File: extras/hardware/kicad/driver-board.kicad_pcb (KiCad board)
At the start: 4 copper layers, 42.8 x 36.8 mm, 49 parts, among them J1 Conn_01x13_Male, U1 TXS0108E, U2 ME6210A30M3G, U3 ME6210A33M3G, U4 TLV61046ADB, U5 NC7SZ125, U6 FT813, U7 ER-TFT040-2, X1 YSX321SL

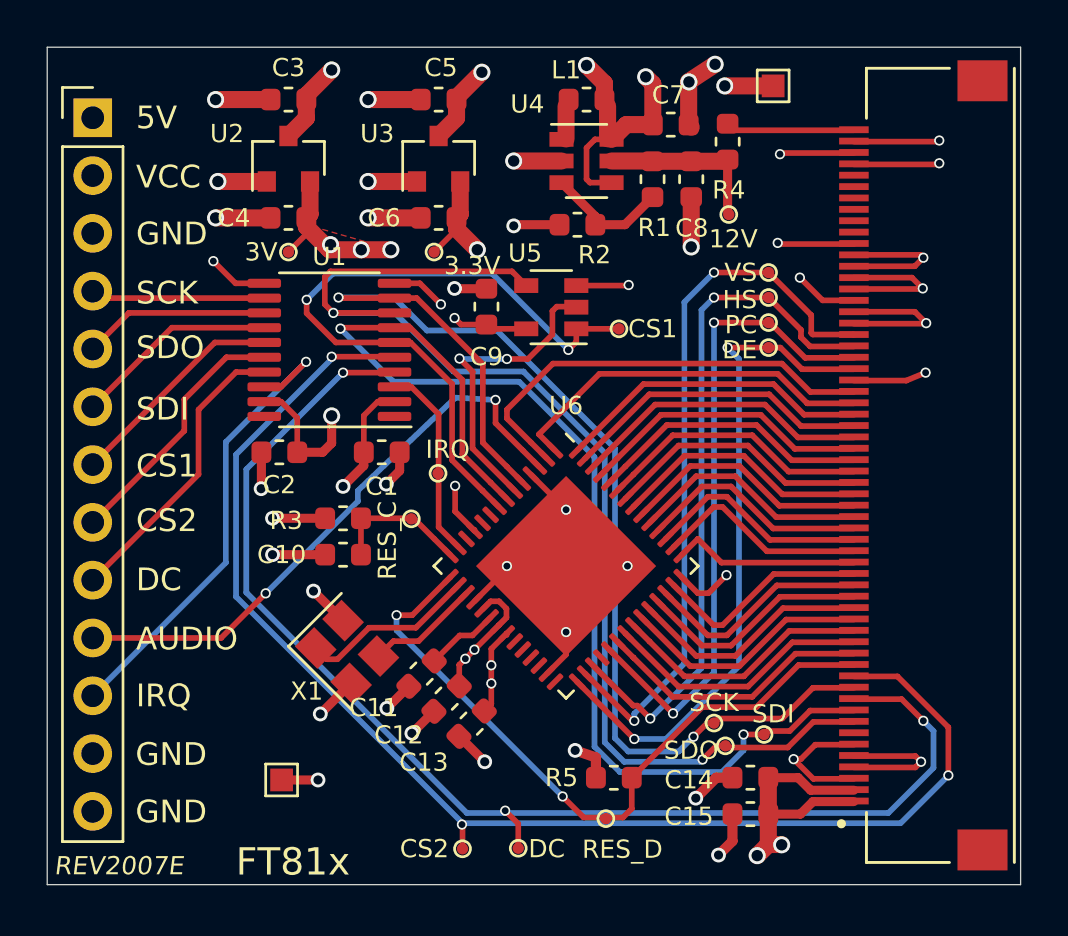
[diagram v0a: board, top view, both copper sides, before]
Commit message: Update board to aisler specs
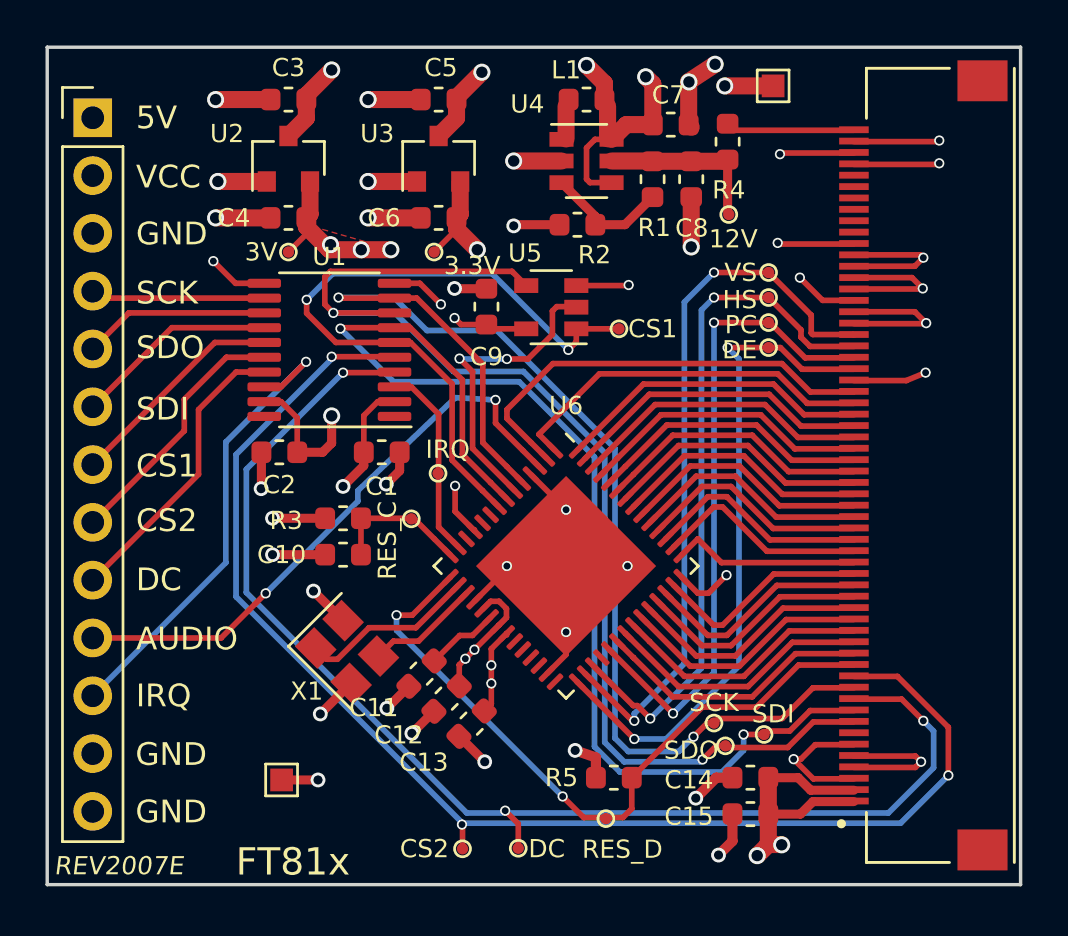
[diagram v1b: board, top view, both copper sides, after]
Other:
- rule pad_to_mask_clearance: 0.05 -> 0
